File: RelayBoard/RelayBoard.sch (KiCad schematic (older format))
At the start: 54 parts, among them J1 Micro_SD_Card, J10 Conn_01x04_Male, J11 Conn_01x04_Male, J12 Conn_01x04_Male, J2 Screw_Terminal_01x02, J3 Conn_01x04_Male, J4 Conn_01x04_Male, J5 Conn_01x04_Male, J6 Conn_01x04_Male, J7 SI-52008-F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

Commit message: finished layout
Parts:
- added C21: 100uF, Capacitor_SMD:C_0603_1608Metric_Pad1.05x0.95mm_HandSolder, symbol Device:C_Small
- added C22: 330uF, Capacitor_SMD:C_0603_1608Metric_Pad1.05x0.95mm_HandSolder, symbol Device:C_Small
- added D2: 1N5822, Diode_THT:D_DO-201AD_P15.24mm_Horizontal, symbol Diode:1N5822
- added JP1: Jumper_NO_Small, Jumper:SolderJumper-2_P1.3mm_Open_Pad1.0x1.5mm, symbol Device:Jumper_NO_Small
- added L1: 330uH, Inductor_SMD:L_0603_1608Metric_Pad1.05x0.95mm_HandSolder, symbol Device:L
- added U5: LM2575-5.0BU, Package_TO_SOT_SMD:TO-263-5_TabPin3, symbol Regulator_Switching:LM2575-5.0BU
- J2: footprint TerminalBlock:TerminalBlock_Altech_AK300-2_P5.00mm -> TerminalBlock_Phoenix:TerminalBlock_Phoenix_MKDS-1,5-2_1x02_P5.00mm_Horizontal
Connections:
- net labels added: +24V, 5V_CAN, RX1+, RX1-, RX2+, RX2-, TX1+, TX1-, TX2+, TX2-
- net labels removed: GND24, RXM1, RXM2, RXP1, RXP2, TXM1, TXM2, TXP1, TXP2
- wire segments 59 -> 62
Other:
- moved on the sheet: C15, C17, C19, J2, J7, R11, R13, R3, R5, R7, R9, U3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

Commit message: Programming connector, CAN connectors 2.54mm
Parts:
- removed J12, J6: Conn_01x04_Male, Connector_PinHeader_1.00mm:PinHeader_1x04_P1.00mm_Vertical, symbol Connector:Conn_01x04_Male
- added J13: Conn_01x04_Male, Connector_PinHeader_2.54mm:PinHeader_1x04_P2.54mm_Vertical, symbol Connector:Conn_01x04_Male
- J10, J11, J3, J4, J5, J9: footprint Connector_PinHeader_1.00mm:PinHeader_1x04_P1.00mm_Vertical -> Connector_JST:JST_XH_B4B-XH-AM_1x04_P2.50mm_Vertical
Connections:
- net labels added: SWCLK, SWDIO
- no-connect marks 87 -> 85
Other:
- moved on the sheet: C21, C22, D2, J1, J2, L1, U3, U4, U5

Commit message: replace pin jumper with solder jumper
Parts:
- removed JP1: Jumper_NO_Small, Jumper:SolderJumper-2_P1.3mm_Open_Pad1.0x1.5mm, symbol Device:Jumper_NO_Small
- added R15: 0Ω, Resistor_SMD:R_0805_2012Metric_Pad1.15x1.40mm_HandSolder, symbol Device:R_Small_US
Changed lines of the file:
@@
 Text GLabel 8600 2800 2    50   Input ~ 0
 5V
-$Comp
-L Device:Jumper_NO_Small JP1
-U 1 1 5E87BCA4
-P 8350 2150
-F 0 "JP1" H 8350 2335 50  0000 C CNN
-F 1 "Jumper_NO_Small" H 8350 2244 50  0000 C CNN
-F 2 "Jumper:SolderJumper-2_P1.3mm_Open_Pad1.0x1.5mm" H 8350 2150 50  0001 C CNN
-F 3 "~" H 8350 2150 50  0001 C CNN
-	1    8350 2150
-	1    0    0    -1
-$EndComp
-Text GLabel 8250 2150 0    50   Input ~ 0
+Text GLabel 7950 2150 0    50   Input ~ 0
 5V_CAN
-Text GLabel 8450 2150 2    50   Input ~ 0
+Text GLabel 8150 2150 2    50   Input ~ 0
 5V
 Text GLabel 1650 6900 0    50   Input ~ 0
@@
 Text GLabel 6700 2050 1    50   Input ~ 0
 GND
+$Comp
+L Device:R_Small_US R15
+U 1 1 5E863A07
+P 8050 2150
+F 0 "R15" V 7845 2150 50  0000 C CNN
+F 1 "0Ω" V 7936 2150 50  0000 C CNN
+F 2 "Resistor_SMD:R_0805_2012Metric_Pad1.15x1.40mm_HandSolder" H 8050 2150 50  0001 C CNN
+F 3 "~" H 8050 2150 50  0001 C CNN
+	1    8050 2150
+	0    1    1    0
+$EndComp
 $EndSCHEMATC

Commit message: better solder jumper pad
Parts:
- R15: footprint Resistor_SMD:R_0805_2012Metric_Pad1.15x1.40mm_HandSolder -> Jumper:SolderJumper-2_P1.3mm_Open_TrianglePad1.0x1.5mm
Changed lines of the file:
@@
 F 0 "R15" V 7845 2150 50  0000 C CNN
 F 1 "0Ω" V 7936 2150 50  0000 C CNN
-F 2 "Resistor_SMD:R_0805_2012Metric_Pad1.15x1.40mm_HandSolder" H 8050 2150 50  0001 C CNN
+F 2 "Jumper:SolderJumper-2_P1.3mm_Open_TrianglePad1.0x1.5mm" H 8050 2150 50  0001 C CNN
 F 3 "~" H 8050 2150 50  0001 C CNN
 	1    8050 2150

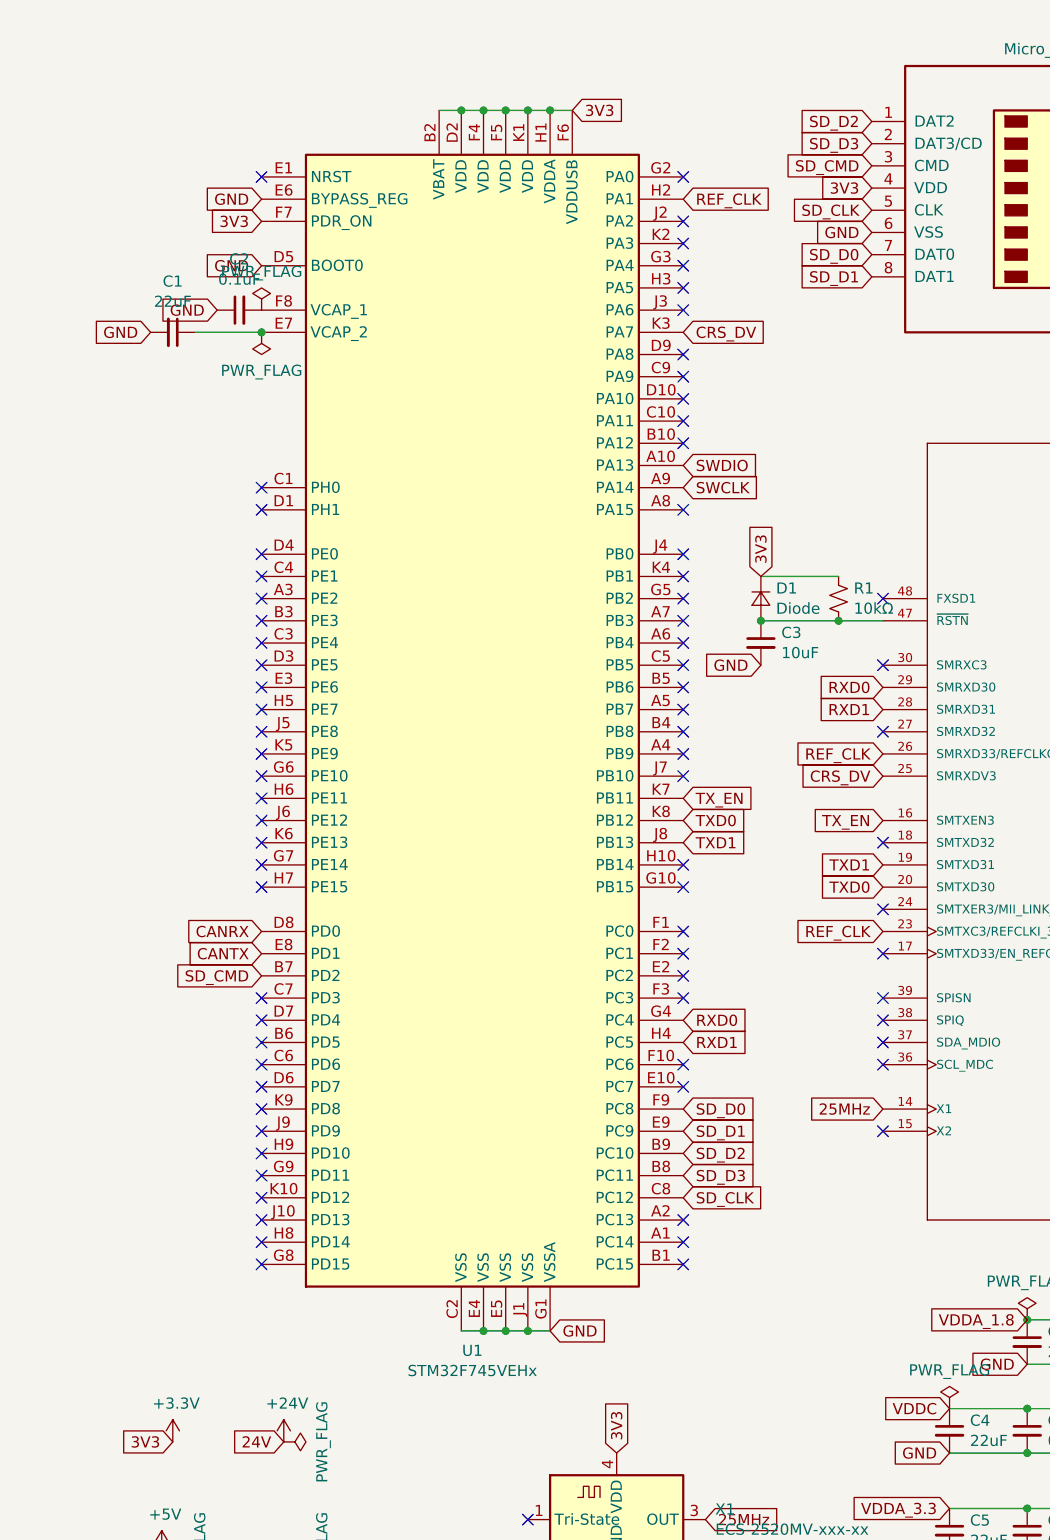
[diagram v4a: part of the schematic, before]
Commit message: substantial rewiring after adding MDIO and MCL
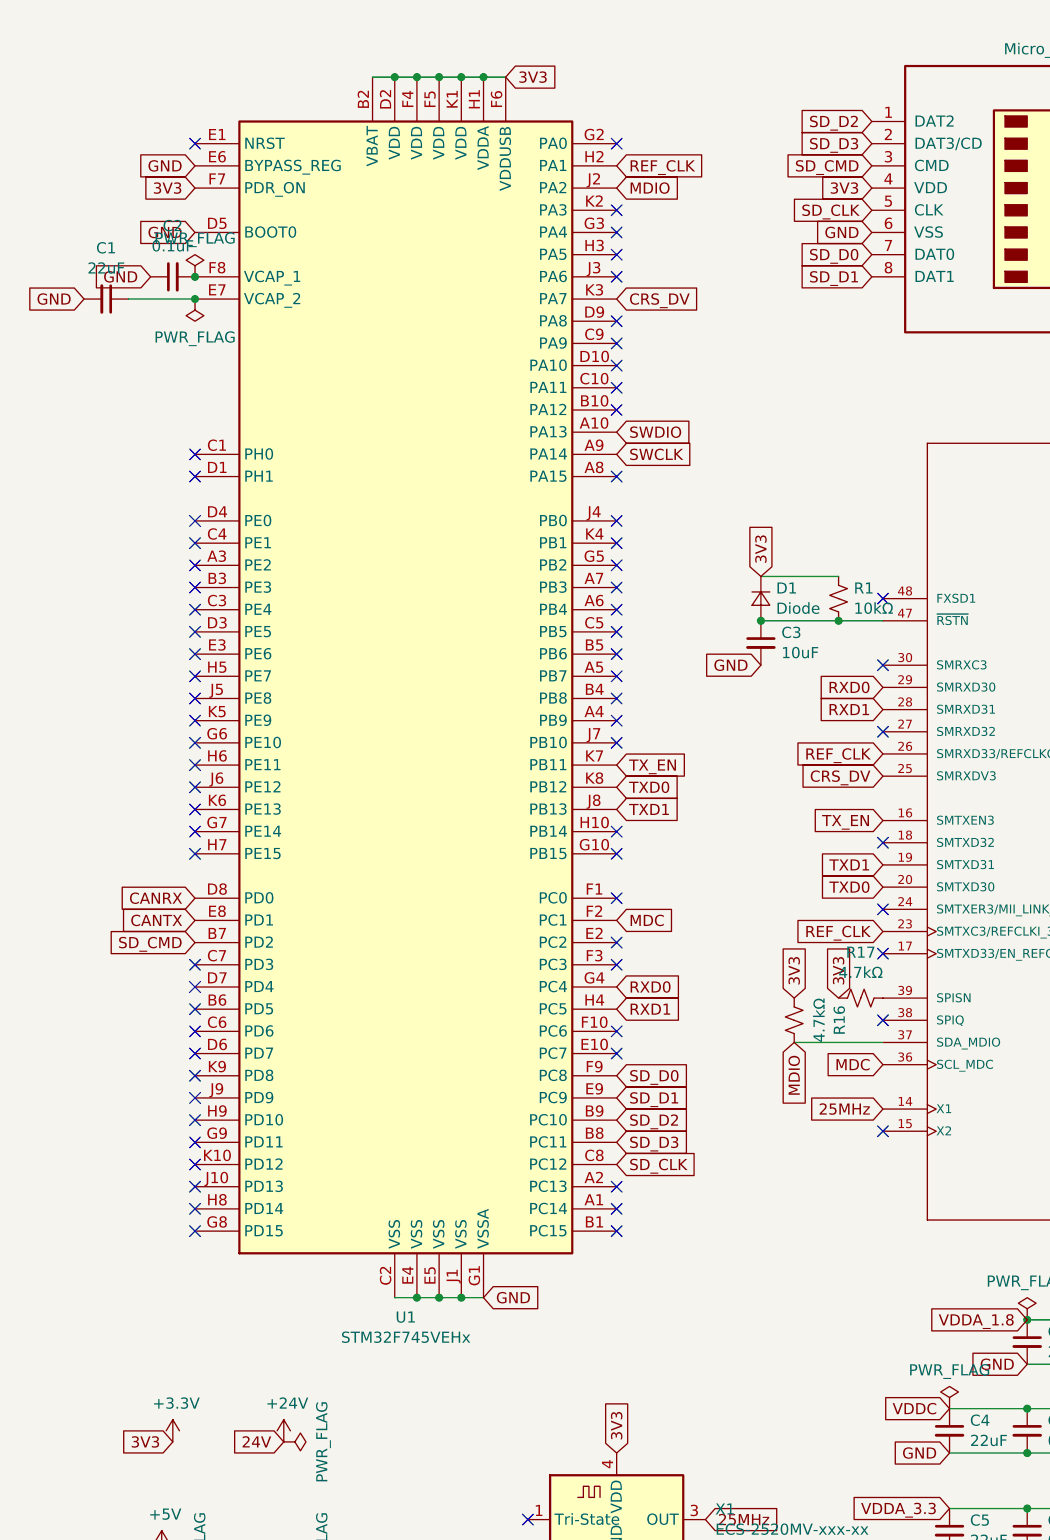
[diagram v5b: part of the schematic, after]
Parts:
- added R16, R17: 4.7kΩ, Resistor_SMD:R_0603_1608Metric_Pad1.05x0.95mm_HandSolder, symbol Device:R_Small_US
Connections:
- net +3V3: now also R16.2, R17.2
- net MDC: now reaches U2.36 (SCL_MDC)
- net MDC: now also U1.F2 (PC1)
- net MDIO: now reaches U2.37 (SDA_MDIO)
- net MDIO: now also U1.J2 (PA2), R16.1
- net at U2.39 (SPISN): now also R17.1
- no-connect marks 85 -> 80
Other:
- moved on the sheet: C1, C2, U1

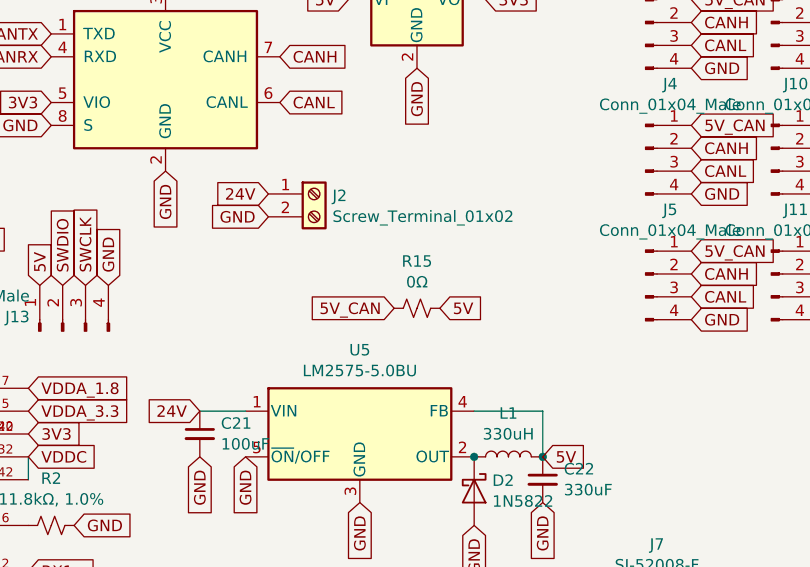
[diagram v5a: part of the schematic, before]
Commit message: add polyfuse, check all RMII stuff, shorten diode trace
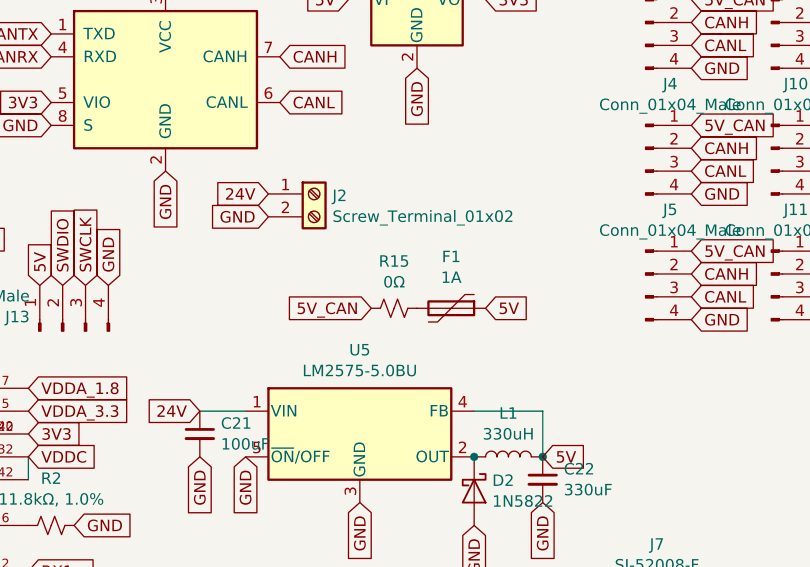
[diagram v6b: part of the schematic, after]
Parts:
- added F1: 1A, Fuse:Fuse_0805_2012Metric_Pad1.15x1.40mm_HandSolder, symbol Device:Polyfuse
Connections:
- net +5V: now also F1.1; no longer R15.1
- new net: F1.2, R15.1
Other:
- moved on the sheet: R15
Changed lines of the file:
@@
 Text GLabel 8600 2800 2    50   Input ~ 0
 5V
-Text GLabel 7950 2150 0    50   Input ~ 0
-5V_CAN
-Text GLabel 8150 2150 2    50   Input ~ 0
-5V
+Text GLabel 7850 2150 0    50   Input ~ 0
+5V_CAN
 Text GLabel 1650 6900 0    50   Input ~ 0
 24V
@@
 L Device:R_Small_US R15
 U 1 1 5E863A07
-P 8050 2150
-F 0 "R15" V 7845 2150 50  0000 C CNN
-F 1 "0Ω" V 7936 2150 50  0000 C CNN
-F 2 "Jumper:SolderJumper-2_P1.3mm_Open_TrianglePad1.0x1.5mm" H 8050 2150 50  0001 C CNN
-F 3 "~" H 8050 2150 50  0001 C CNN
-	1    8050 2150
+P 7950 2150
+F 0 "R15" V 7745 2150 50  0000 C CNN
+F 1 "0Ω" V 7836 2150 50  0000 C CNN
+F 2 "Jumper:SolderJumper-2_P1.3mm_Open_TrianglePad1.0x1.5mm" H 7950 2150 50  0001 C CNN
+F 3 "~" H 7950 2150 50  0001 C CNN
+	1    7950 2150
 	0    1    1    0
 $EndComp
@@
 	3950 5100 4350 5100
 NoConn ~ 4350 5500
+Text GLabel 8350 2150 2    50   Input ~ 0
+5V
+$Comp
+L Device:Polyfuse F1
+U 1 1 5EA76ED7
+P 8200 2150
+F 0 "F1" V 7975 2150 50  0000 C CNN
+F 1 "1A" V 8066 2150 50  0000 C CNN
+F 2 "Fuse:Fuse_0805_2012Metric_Pad1.15x1.40mm_HandSolder" H 8250 1950 50  0001 L CNN
+F 3 "~" H 8200 2150 50  0001 C CNN
+	1    8200 2150
+	0    1    1    0
+$EndComp
 $EndSCHEMATC

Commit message: partial rework of power - needs some bigger components oops
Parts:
- removed D2: 1N5822, Diode_THT:D_DO-201AD_P15.24mm_Horizontal, symbol Diode:1N5822
- added C23: 470uF EMZS350ARA471MHA0G, Capacitor_SMD:CP_Elec_10x10, symbol Device:CP1_Small
- added D2: CCS15F40L3FTR-ND, Diode_SMD:D_0603_1608Metric_Pad1.05x0.95mm_HandSolder, symbol Device:D_Schottky
- added L2: 22uH PA4320, Inductor_SMD:L_Pulse_PA4320, symbol Device:L
- C21: value 100uF -> 470uF EMZS350ARA471MHA0G; footprint Capacitor_SMD:C_0603_1608Metric_Pad1.05x0.95mm_HandSolder -> Capacitor_SMD:CP_Elec_10x10; symbol Device:C_Small -> Device:CP1_Small
- C22: value 330uF -> 330uF EMZS350ARA331MHA0G; footprint Capacitor_SMD:C_0603_1608Metric_Pad1.05x0.95mm_HandSolder -> Capacitor_SMD:CP_Elec_10x10; symbol Device:C_Small -> Device:CP1_Small
- L1: value 330uH -> 330uH PA4320; footprint Inductor_SMD:L_0603_1608Metric_Pad1.05x0.95mm_HandSolder -> Inductor_SMD:L_Pulse_PA4320
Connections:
- net +5V: now also C23.1, L2.2; no longer C22.1, L1.2, U5.4 (FB)
- net GND: now also C23.2, D2.2 (A)
- net at L1.1, U5.2 (OUT): now also D2.1 (K)
- new net: C22.1, L1.2, L2.1, U5.4 (FB)
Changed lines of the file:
@@
 RX2-
 $Comp
-L Device:C_Small C21
+L Device:CP1_Small C21
 U 1 1 5E84FFB9
 P 7100 2700
 F 0 "C21" H 7192 2746 50  0000 L CNN
-F 1 "100uF" H 7192 2655 50  0000 L CNN
-F 2 "Capacitor_SMD:C_0603_1608Metric_Pad1.05x0.95mm_HandSolder" H 7100 2700 50  0001 C CNN
+F 1 "470uF EMZS350ARA471MHA0G" H 7192 2655 50  0000 L CNN
+F 2 "Capacitor_SMD:CP_Elec_10x10" H 7100 2700 50  0001 C CNN
 F 3 "~" H 7100 2700 50  0001 C CNN
 	1    7100 2700
@@
 GND
 $Comp
-L Diode:1N5822 D2
-U 1 1 5E8672B7
-P 8300 2950
-F 0 "D2" V 8254 3029 50  0000 L CNN
-F 1 "1N5822" V 8345 3029 50  0000 L CNN
-F 2 "Diode_THT:D_DO-201AD_P15.24mm_Horizontal" H 8300 2775 50  0001 C CNN
-F 3 "http://www.vishay.com/docs/88526/1n5820.pdf" H 8300 2950 50  0001 C CNN
-	1    8300 2950
-	0    1    1    0
-$EndComp
-Connection ~ 8300 2800
-$Comp
 L Device:L L1
 U 1 1 5E8687D9
 P 8450 2800
 F 0 "L1" V 8640 2800 50  0000 C CNN
-F 1 "330uH" V 8549 2800 50  0000 C CNN
-F 2 "Inductor_SMD:L_0603_1608Metric_Pad1.05x0.95mm_HandSolder" H 8450 2800 50  0001 C CNN
+F 1 "330uH PA4320" V 8549 2800 50  0000 C CNN
+F 2 "Inductor_SMD:L_Pulse_PA4320" H 8450 2800 50  0001 C CNN
 F 3 "~" H 8450 2800 50  0001 C CNN
 	1    8450 2800
@@
 $EndComp
 $Comp
-L Device:C_Small C22
+L Device:CP1_Small C22
 U 1 1 5E86EE8D
 P 8600 2900
 F 0 "C22" H 8692 2946 50  0000 L CNN
-F 1 "330uF" H 8692 2855 50  0000 L CNN
-F 2 "Capacitor_SMD:C_0603_1608Metric_Pad1.05x0.95mm_HandSolder" H 8600 2900 50  0001 C CNN
+F 1 "330uF EMZS350ARA331MHA0G" H 8692 2855 50  0000 L CNN
+F 2 "Capacitor_SMD:CP_Elec_10x10" H 8600 2900 50  0001 C CNN
 F 3 "~" H 8600 2900 50  0001 C CNN
 	1    8600 2900
@@
 Text GLabel 8600 3000 3    50   Input ~ 0
 GND
-Text GLabel 8600 2800 2    50   Input ~ 0
-5V
 Text GLabel 7850 2150 0    50   Input ~ 0
 5V_CAN
@@
 	0    1    1    0
 $EndComp
+Text GLabel 8900 2800 2    50   Input ~ 0
+5V
+$Comp
+L Device:L L2
+U 1 1 5EA957DB
+P 8750 2800
+F 0 "L2" V 8940 2800 50  0000 C CNN
+F 1 "22uH PA4320" V 8849 2800 50  0000 C CNN
+F 2 "Inductor_SMD:L_Pulse_PA4320" H 8750 2800 50  0001 C CNN
+F 3 "~" H 8750 2800 50  0001 C CNN
+	1    8750 2800
+	0    -1   -1   0
+$EndComp
+Text GLabel 8900 3000 3    50   Input ~ 0
+GND
+$Comp
+L Device:D_Schottky D2
+U 1 1 5EA9FF6A
+P 8300 2950
+F 0 "D2" V 8254 3029 50  0000 L CNN
+F 1 "CCS15F40L3FTR-ND" V 8345 3029 50  0000 L CNN
+F 2 "Diode_SMD:D_0603_1608Metric_Pad1.05x0.95mm_HandSolder" H 8300 2950 50  0001 C CNN
+F 3 "~" H 8300 2950 50  0001 C CNN
+	1    8300 2950
+	0    1    1    0
+$EndComp
+Connection ~ 8300 2800
+$Comp
+L Device:CP1_Small C23
+U 1 1 5EA957E1
+P 8900 2900
+F 0 "C23" H 8992 2946 50  0000 L CNN
+F 1 "470uF EMZS350ARA471MHA0G" H 8992 2855 50  0000 L CNN
+F 2 "Capacitor_SMD:CP_Elec_10x10" H 8900 2900 50  0001 C CNN
+F 3 "~" H 8900 2900 50  0001 C CNN
+	1    8900 2900
+	1    0    0    -1
+$EndComp
 $EndSCHEMATC
